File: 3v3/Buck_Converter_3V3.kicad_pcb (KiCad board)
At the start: 2 copper layers, 52 x 15 mm, 16 parts, among them P1 CONN_2, P2 CONN_2, U1 LM2597

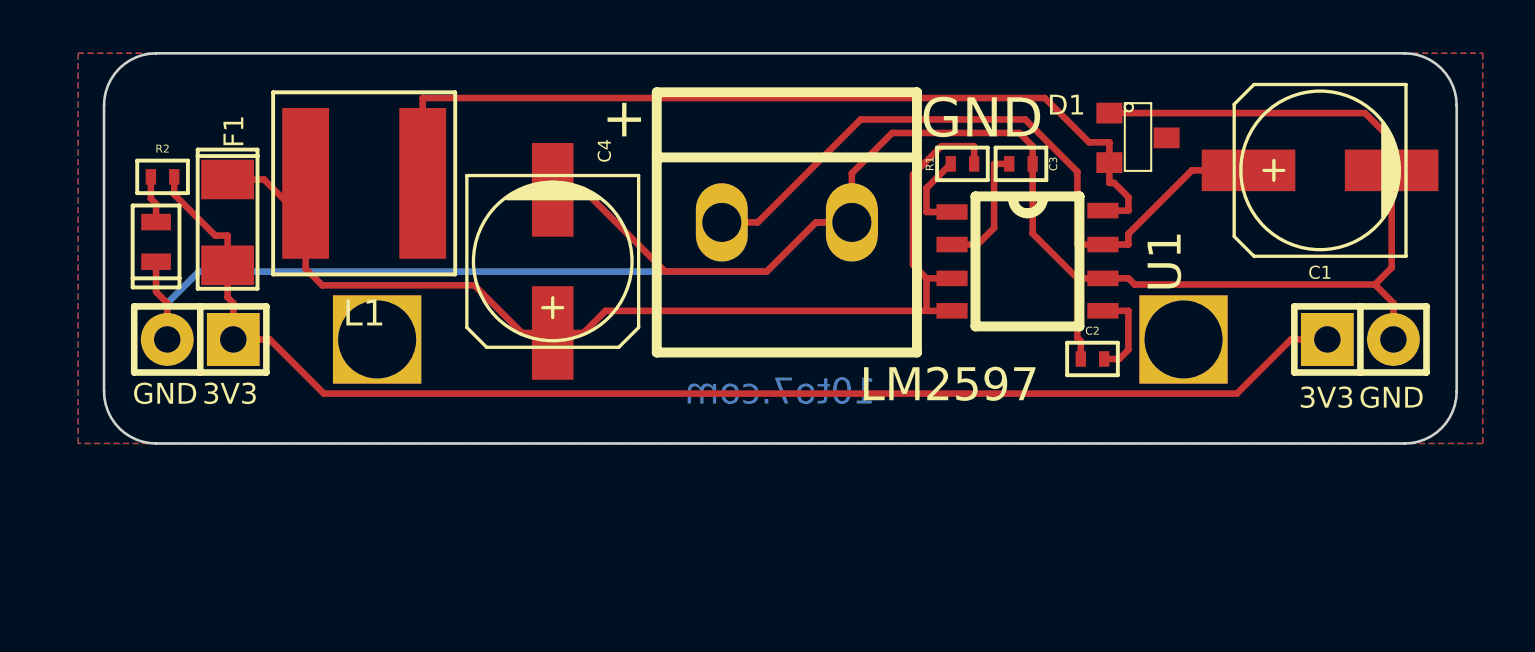
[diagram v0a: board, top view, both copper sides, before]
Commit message: Added additional pin input
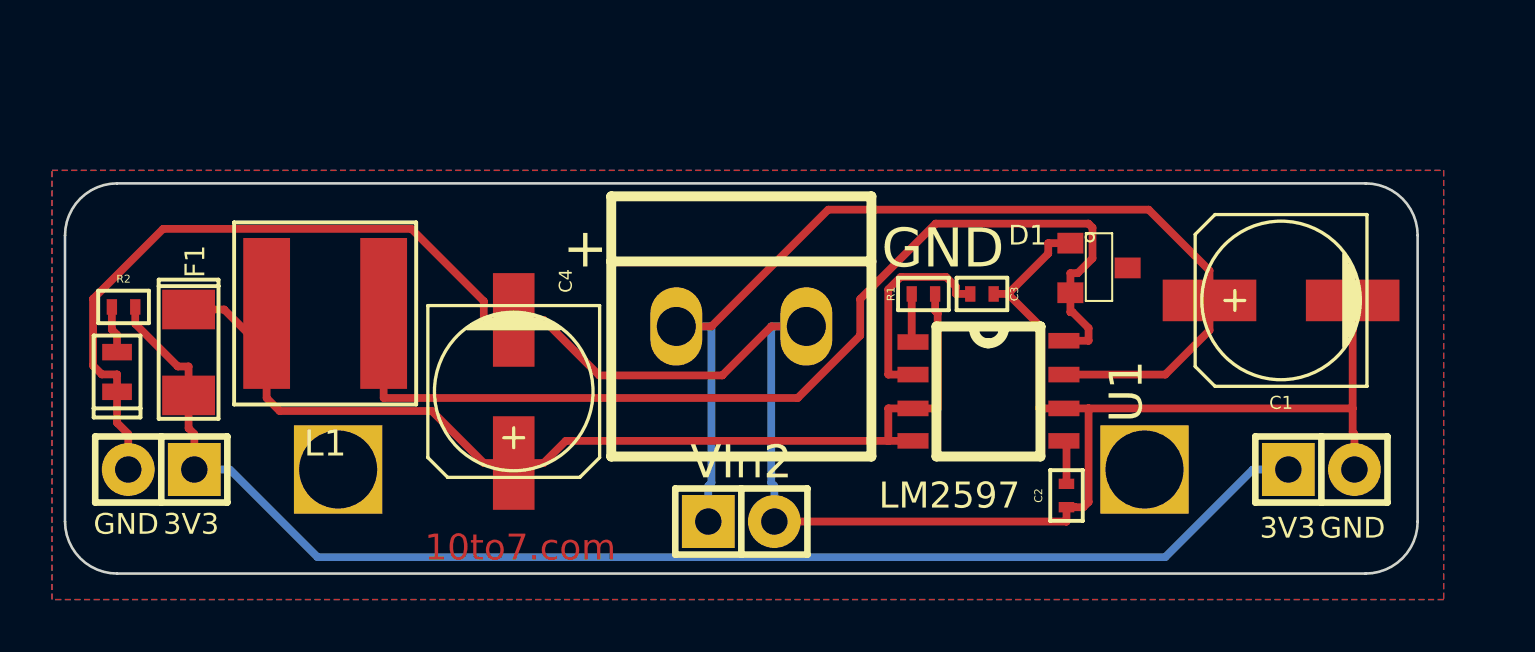
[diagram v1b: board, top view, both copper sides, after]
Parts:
- added VIn2: CONN_2, Pin_Headers:Pin_Header_Straight_1x02, F.Cu at (144.4, 97.6)
- moved C2 5.34 mm to (156.9, 96.6), turned to 270 degrees
- moved 3mmHole 5.22 mm to (129.4, 91.6)
- moved 3mmHole_1 5.22 mm to (160.9, 97.6)
- moved C1 5.22 mm to (165.1, 89.1)
- moved C3 5.22 mm to (153.6, 88.8)
- moved C4 5.22 mm to (135.6, 92.6)
- moved D1 5.22 mm to (158.1, 87.8)
- moved D2 5.22 mm to (120.4, 91.8)
- moved F1 5.22 mm to (123.1, 91.1)
- moved L1 5.22 mm to (128.4, 89.6)
- moved P1 5.22 mm to (166.7, 95.6)
- moved P2 5.22 mm to (122.1, 95.6)
- moved R1 5.22 mm to (151.4, 88.8)
- moved R2 5.22 mm to (120.6, 89.3)
- moved U1 5.22 mm to (153.9, 92.6)
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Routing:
- net +12V: track 26.9 -> 40.8 mm
- net Net-(D1-Pad2): track 34.4 -> 40.3 mm
- net GND: track 95.4 -> 92.2 mm
- net Net-(C3-Pad1): track 4.93 -> 8.00 mm
- net /Feedback: track 42.8 -> 40.5 mm
- net /Shutdown_Soft-start: track 3.56 -> 1.69 mm
- net /Error_Flag: track 3.22 -> 1.87 mm
- net +3.3V: track 51.3 -> 52.3 mm
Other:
- net class Default: clearance 0 -> 0.2; trace_width 0.254 -> 0.3
- rule trace_clearance: 0 -> 0.2

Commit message: missed the final changes to the PCB from last commit.
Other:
- board text added: "5V Vcc ■ 3V3 Vcc ■"
- board text added: "VCC"
- board text removed: "3V3"
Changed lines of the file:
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@@
     (links 27)
     (no_connects 0)
-    (area 119.824999 79.549999 171.925001 94.650001)
+    (area 117.875 77.7 171.375001 112.300001)
     (thickness 1.6)
-    (drawings 25)
+    (drawings 26)
     (tracks 115)
     (zones 0)
@@
   (page A4)
   (layers
-    (15 F.Cu signal)
+    (15 F.Cu signal hide)
     (0 B.Cu signal)
     (16 B.Adhes user)
@@
     (descr "1 pin")
     (tags "CONN DEV")
-    (fp_text reference VIn2 (at 0 -2.286) (layer F.SilkS)
-      (effects (font (size 1.27 1.27) (thickness 0.2032)))
+    (fp_text reference VIn2 (at -0.25 -1.75) (layer F.SilkS)
+      (effects (font (size 0.6 0.6) (thickness 0.15)))
     )
     (fp_text value CONN_2 (at 0 0) (layer F.SilkS) hide
@@
       (rotate (xyz 0 0 0))
     )
+  )
+  (gr_text "5V Vcc ■\n3V3 Vcc ■" (at 122.375 88.1) (layer B.SilkS)
+    (effects (font (size 1.5 1.5) (thickness 0.3)) (justify right mirror))
   )
   (dimension 21 (width 0.3) (layer Dwgs.User)
@@
     (effects (font (size 0.8 0.8) (thickness 0.2)) (justify mirror))
   )
-  (gr_text 3V3 (at 123.225 97.7) (layer B.SilkS)
+  (gr_text VCC (at 123.225 97.7) (layer B.SilkS)
     (effects (font (size 0.8 0.8) (thickness 0.2)) (justify mirror))
   )
-  (gr_text 3V3 (at 123.225 97.7) (layer F.SilkS)
+  (gr_text VCC (at 123.225 97.7) (layer F.SilkS)
     (effects (font (size 0.8 0.8) (thickness 0.2)))
   )
@@
     (effects (font (size 0.8 0.8) (thickness 0.2)))
   )
-  (gr_text 3V3 (at 165.375 97.85) (layer B.SilkS)
+  (gr_text VCC (at 165.375 97.85) (layer B.SilkS)
     (effects (font (size 0.8 0.8) (thickness 0.2)) (justify mirror))
   )
@@
     (effects (font (size 0.8 0.8) (thickness 0.2)) (justify mirror))
   )
-  (gr_text 3V3 (at 165.375 97.85) (layer F.SilkS)
+  (gr_text VCC (at 165.375 97.85) (layer F.SilkS)
     (effects (font (size 0.8 0.8) (thickness 0.2)))
   )
